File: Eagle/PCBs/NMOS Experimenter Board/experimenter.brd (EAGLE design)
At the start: 77.5 x 99.1 mm, 1209 parts, among them Q10 2N7002, Q11 2N7002, Q12 2N7002, Q13 2N7002, Q14 2N7002, Q15 2N7002, Q16 2N7002, Q17 2N7002, Q18 2N7002, Q19 2N7002, Q2 2N7002, Q20 2N7002, Q21 2N7002, Q22 2N7002, Q23 2N7002, Q24 2N7002, Q25 2N7002, Q26 2N7002, Q27 2N7002, Q28 2N7002, Q29 2N7002, Q3 2N7002, Q30 2N7002, Q31 2N7002, Q32 2N7002, Q33 2N7002, Q34 2N7002, Q35 2N7002, Q36 2N7002, Q37 2N7002, Q38 2N7002, Q39 2N7002, Q4 2N7002, Q40 2N7002, Q41 2N7002, Q42 2N7002, Q43 2N7002, Q44 2N7002, Q45 2N7002, Q46 2N7002, Q47 2N7002, Q48 2N7002, Q49 2N7002, Q5 2N7002, Q50 2N7002, Q51 2N7002, Q52 2N7002, Q53 2N7002, Q54 2N7002, Q55 2N7002, Q56 2N7002, Q57 2N7002, Q58 2N7002, Q59 2N7002, Q6 2N7002, Q60 2N7002, Q61 2N7002, Q62 2N7002, Q63 2N7002, Q64 2N7002, Q65 2N7002, Q66 2N7002, Q67 2N7002, Q68 2N7002, Q69 2N7002, Q7 2N7002, Q70 2N7002, Q71 2N7002, Q72 2N7002, Q73 2N7002, Q8 2N7002, Q9 2N7002, U1 74HC14PW, U2 74HC14PW

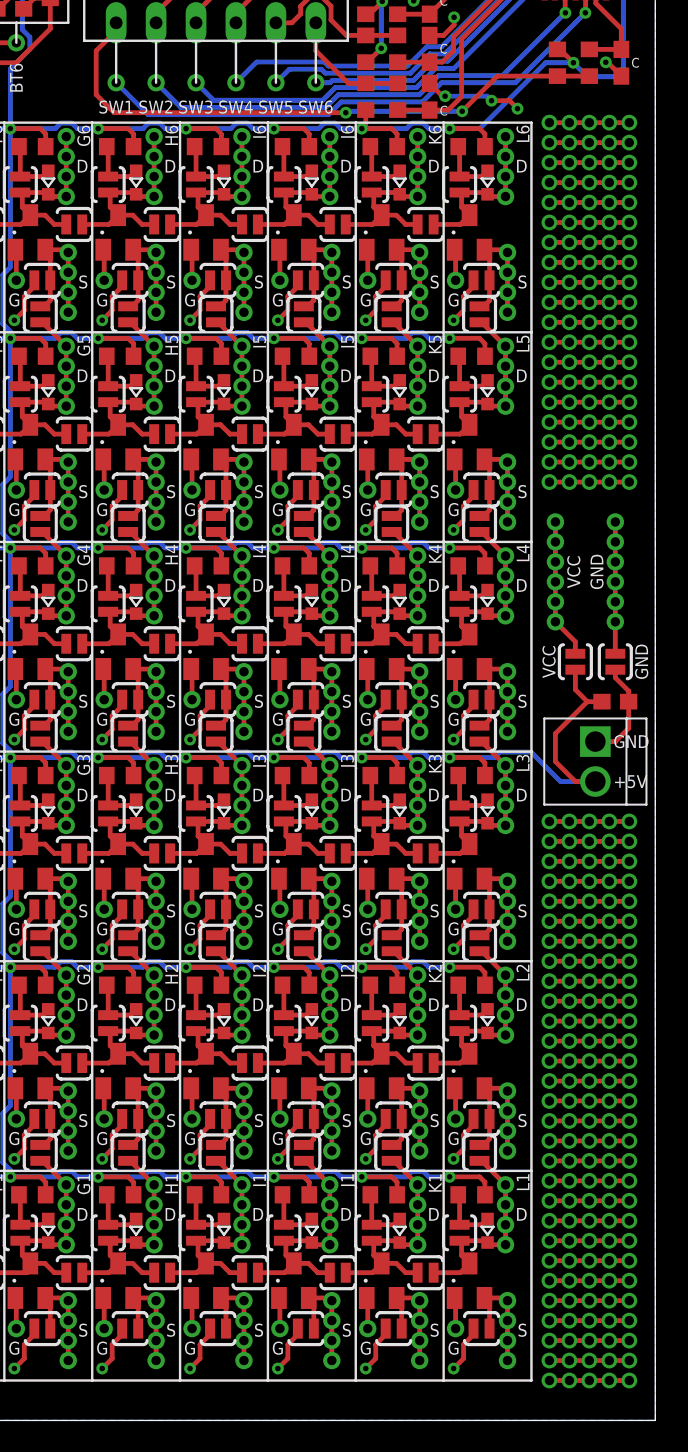
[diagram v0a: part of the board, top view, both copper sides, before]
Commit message: Added amazing protoboard area.
https://www.eevblog.com/forum/manufacture/improved-protoboardperfboard-for-direct-soic-mounting/
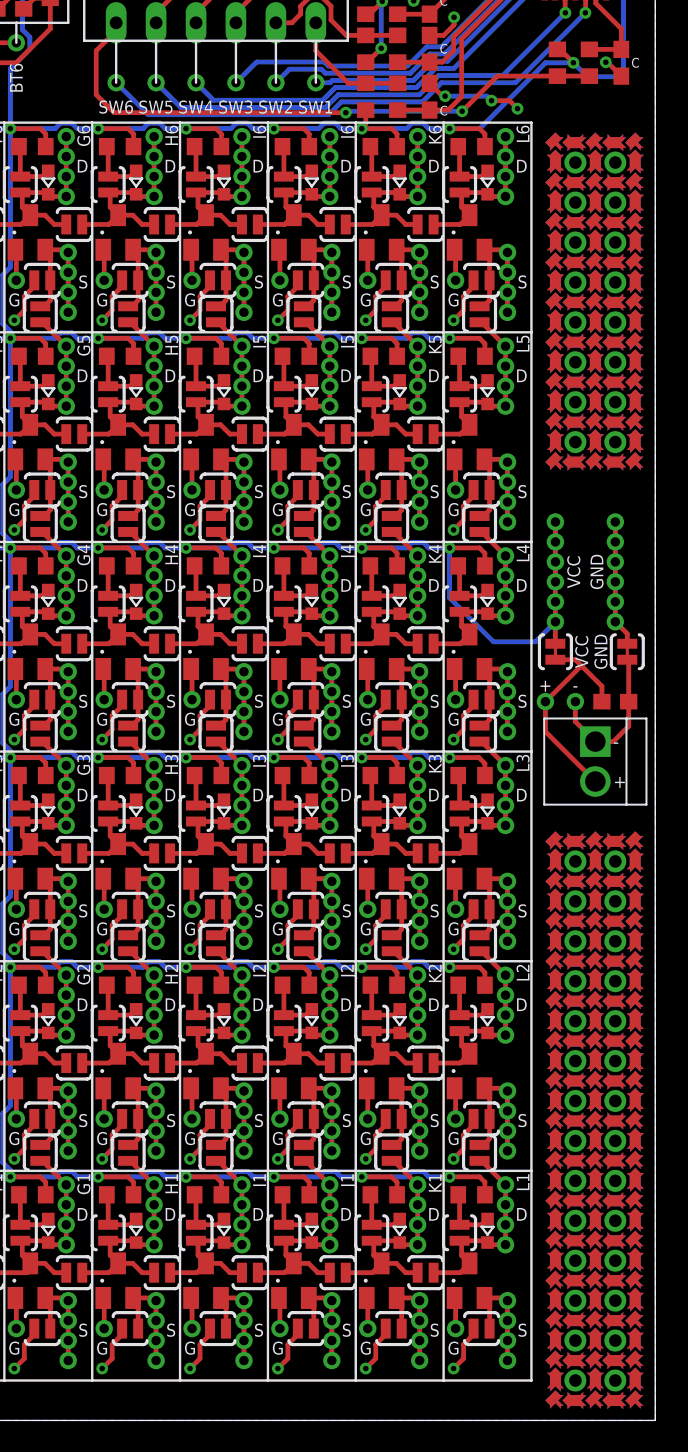
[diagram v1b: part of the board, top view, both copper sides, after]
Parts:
- added U$1, U$101, U$105, U$109, U$113, U$117, U$121, U$125, U$162, U$166, U$170, U$174, U$182, U$186, U$190, U$194, U$198, U$202, U$206, U$21, U$210, U$214, U$218, U$222, U$226, U$25, U$29, U$33, U$37, U$41, U$45, U$49, U$53, U$57, U$61, U$65, U$69, U$73, U$77, U$81, U$85, U$89, U$93, U$97: PROTOPADTHT, ellajameson-core:PROTOPAD-THT
- added U$10, U$100, U$104, U$108, U$112, U$116, U$12, U$120, U$124, U$128, U$130, U$132, U$134, U$136, U$138, U$14, U$140, U$142, U$144, U$145, U$147, U$149, U$151, U$153, U$154, U$156, U$158, U$16, U$160, U$165, U$169, U$173, U$177, U$178, U$18, U$180, U$185, U$189, U$193, U$197, U$20, U$201, U$205, U$209, U$213, U$217, U$221, U$225, U$229, U$230, U$24, U$28, U$32, U$36, U$4, U$40, U$44, U$48, U$52, U$56, U$6, U$60, U$64, U$68, U$72, U$76, U$8, U$80, U$84, U$88, U$92, U$96: (no value), ellajameson-core:PROTOPAD-CENTER
- added U$102, U$103, U$106, U$107, U$11, U$110, U$111, U$114, U$115, U$118, U$119, U$122, U$123, U$126, U$127, U$129, U$13, U$131, U$133, U$135, U$137, U$139, U$141, U$143, U$146, U$148, U$15, U$150, U$152, U$155, U$157, U$159, U$161, U$163, U$164, U$167, U$168, U$17, U$171, U$172, U$175, U$176, U$179, U$181, U$183, U$184, U$187, U$188, U$19, U$191, U$192, U$195, U$196, U$199, U$2, U$200, U$203, U$204, U$207, U$208, U$211, U$212, U$215, U$216, U$219, U$22, U$220, U$223, U$224, U$227, U$228, U$23, U$26, U$27, U$3, U$30, U$31, U$34, U$35, U$38, U$39, U$42, U$43, U$46, U$47, U$5, U$50, U$51, U$54, U$55, U$58, U$59, U$62, U$63, U$66, U$67, U$7, U$70, U$71, U$74, U$75, U$78, U$79, U$82, U$83, U$86, U$87, U$9, U$90, U$91, U$94, U$95, U$98, U$99: (no value), ellajameson-core:PROTOPAD-BETWEEN
- added VIN+1, VIN-1: TPWIRE, ellajameson-core:TP_TH_WIRE
- SJ1, SJ2: value SJ_NO -> SJ_NC; device ellajameson-core:SJ_2S-NO -> ellajameson-core:SJ_2S-TRACE
- moved SJ1 3.86 mm to (71.1, 48.9), turned to 90 degrees
- moved SJ2 3.36 mm to (75.7, 48.9)
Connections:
- removed net N$303: SJ2.2, VCC1.TP, VCC2.TP, VCC3.TP, VCC4.TP, VCC5.TP, VCC6.TP
- removed net N$304: SJ1.1, VSS1.TP, VSS2.TP, VSS3.TP, VSS4.TP, VSS5.TP, VSS6.TP
- new net N$321: C4.1, J1.P$1, SJ2.1, VIN-1.TP
- new net N$322: C4.2, J1.P$2, SJ1.1, VIN+1.TP
- net GND: now also SJ2.2, VSS1.TP, VSS2.TP, VSS3.TP, VSS4.TP, VSS5.TP, VSS6.TP; no longer C4.1, J1.P$1, SJ1.2
- net VCC: now also SJ1.2, VCC1.TP, VCC2.TP, VCC3.TP, VCC4.TP, VCC5.TP, VCC6.TP; no longer C4.2, J1.P$2, SJ2.1
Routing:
- net N$322: track 0.00 -> 14.3 mm
- net N$321: track 0.00 -> 9.86 mm
- net N$303: track 8.91 -> 0.00 mm
- net N$304: track 8.38 -> 0.00 mm
- net BB9: track 5.08 -> 0.00 mm, vias 5 -> 0
- net BB8: track 5.08 -> 0.00 mm, vias 5 -> 0
- net BB7: track 5.08 -> 0.00 mm, vias 5 -> 0
- net BB6: track 5.08 -> 0.00 mm, vias 5 -> 0
- net BB5: track 5.08 -> 0.00 mm, vias 5 -> 0
- net BB48: track 5.08 -> 0.00 mm, vias 5 -> 0
- net BB47: track 5.08 -> 0.00 mm, vias 5 -> 0
- net BB46: track 5.08 -> 0.00 mm, vias 5 -> 0
- net BB45: track 5.08 -> 0.00 mm, vias 5 -> 0
- net BB44: track 5.08 -> 0.00 mm, vias 5 -> 0
- net BB43: track 5.08 -> 0.00 mm, vias 5 -> 0
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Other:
- board text added: "+"
- board text added: "-"
- board text removed: "+5V"

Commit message: Start rework on experimenter
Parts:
- removed C10, C12, C13, C14, C15, C6, C8: 0.1u, ellajameson-core:C0603
- removed D10, D11, D12, D13, D14, D15, D16, D17, D18, D19, D2, D20, D21, D22, D23, D24, D25, D26, D27, D28, D29, D3, D30, D31, D32, D33, D34, D35, D36, D37, D38, D39, D4, D40, D41, D42, D43, D44, D45, D46, D47, D48, D49, D5, D50, D51, D52, D53, D54, D55, D56, D57, D58, D59, D6, D60, D61, D62, D63, D64, D65, D66, D67, D68, D69, D7, D70, D71, D72, D73, D8, D9: (no value), ellajameson-core:CHIP-LED0603
- removed DRAINA10, DRAINA11, DRAINA12, DRAINA13, DRAINA14, DRAINA15, DRAINA16, DRAINA17, DRAINA18, DRAINA19, DRAINA2, DRAINA20, DRAINA21, DRAINA22, DRAINA23, DRAINA24, DRAINA25, DRAINA26, DRAINA27, DRAINA28, DRAINA29, DRAINA3, DRAINA30, DRAINA31, DRAINA32, DRAINA33, DRAINA34, DRAINA35, DRAINA36, DRAINA37, DRAINA38, DRAINA39, DRAINA4, DRAINA40, DRAINA41, DRAINA42, DRAINA43, DRAINA44, DRAINA45, DRAINA46, DRAINA47, DRAINA48, DRAINA49, DRAINA5, DRAINA50, DRAINA51, DRAINA52, DRAINA53, DRAINA54, DRAINA55, DRAINA56, DRAINA57, DRAINA58, DRAINA59, DRAINA6, DRAINA60, DRAINA61, DRAINA62, DRAINA63, DRAINA64, DRAINA65, DRAINA66, DRAINA67, DRAINA68, DRAINA69, DRAINA7, DRAINA70, DRAINA71, DRAINA72, DRAINA73, DRAINA8, DRAINA9, DRAINB10, DRAINB11, DRAINB12, DRAINB13, DRAINB14, DRAINB15, DRAINB16, DRAINB17, DRAINB18, DRAINB19, DRAINB2, DRAINB20, DRAINB21, DRAINB22, DRAINB23, DRAINB24, DRAINB25, DRAINB26, DRAINB27, DRAINB28, DRAINB29, DRAINB3, DRAINB30, DRAINB31, DRAINB32, DRAINB33, DRAINB34, DRAINB35, DRAINB36, DRAINB37, DRAINB38, DRAINB39, DRAINB4, DRAINB40, DRAINB41, DRAINB42, DRAINB43, DRAINB44, DRAINB45, DRAINB46, DRAINB47, DRAINB48, DRAINB49, DRAINB5, DRAINB50, DRAINB51, DRAINB52, DRAINB53, DRAINB54, DRAINB55, DRAINB56, DRAINB57, DRAINB58, DRAINB59, DRAINB6, DRAINB60, DRAINB61, DRAINB62, DRAINB63, DRAINB64, DRAINB65, DRAINB66, DRAINB67, DRAINB68, DRAINB69, DRAINB7, DRAINB70, DRAINB71, DRAINB72, DRAINB73, DRAINB8, DRAINB9, DRAINC10, DRAINC11, DRAINC12, DRAINC13, DRAINC14, DRAINC15, DRAINC16, DRAINC17, DRAINC18, DRAINC19, DRAINC2, DRAINC20, DRAINC21, DRAINC22, DRAINC23, DRAINC24, DRAINC25, DRAINC26, DRAINC27, DRAINC28, DRAINC29, DRAINC3, DRAINC30, DRAINC31, DRAINC32, DRAINC33, DRAINC34, DRAINC35, DRAINC36, DRAINC37, DRAINC38, DRAINC39, DRAINC4, DRAINC40, DRAINC41, DRAINC42, DRAINC43, DRAINC44, DRAINC45, DRAINC46, DRAINC47, DRAINC48, DRAINC49, DRAINC5, DRAINC50, DRAINC51, DRAINC52, DRAINC53, DRAINC54, DRAINC55, DRAINC56, DRAINC57, DRAINC58, DRAINC59, DRAINC6, DRAINC60, DRAINC61, DRAINC62, DRAINC63, DRAINC64, DRAINC65, DRAINC66, DRAINC67, DRAINC68, DRAINC69, DRAINC7, DRAINC70, DRAINC71, DRAINC72, DRAINC73, DRAINC8, DRAINC9, DRAIND10, DRAIND11, DRAIND12, DRAIND13, DRAIND14, DRAIND15, DRAIND16, DRAIND17, DRAIND18, DRAIND19, DRAIND2, DRAIND20, DRAIND21, DRAIND22, DRAIND23, DRAIND24, DRAIND25, DRAIND26, DRAIND27, DRAIND28, DRAIND29, DRAIND3, DRAIND30, DRAIND31, DRAIND32, DRAIND33, DRAIND34, DRAIND35, DRAIND36, DRAIND37, DRAIND38, DRAIND39, DRAIND4, DRAIND40, DRAIND41, DRAIND42, DRAIND43, DRAIND44, DRAIND45, DRAIND46, DRAIND47, DRAIND48, DRAIND49, DRAIND5, DRAIND50, DRAIND51, DRAIND52, DRAIND53, DRAIND54, DRAIND55, DRAIND56, DRAIND57, DRAIND58, DRAIND59, DRAIND6, DRAIND60, DRAIND61, DRAIND62, DRAIND63, DRAIND64, DRAIND65, DRAIND66, DRAIND67, DRAIND68, DRAIND69, DRAIND7, DRAIND70, DRAIND71, DRAIND72, DRAIND73, DRAIND8, DRAIND9, GATE10, GATE11, GATE12, GATE13, GATE14, GATE15, GATE16, GATE17, GATE18, GATE19, GATE2, GATE20, GATE21, GATE22, GATE23, GATE24, GATE25, GATE26, GATE27, GATE28, GATE29, GATE3, GATE30, GATE31, GATE32, GATE33, GATE34, GATE35, GATE36, GATE37, GATE38, GATE39, GATE4, GATE40, GATE41, GATE42, GATE43, GATE44, GATE45, GATE46, GATE47, GATE48, GATE49, GATE5, GATE50, GATE51, GATE52, GATE53, GATE54, GATE55, GATE56, GATE57, GATE58, GATE59, GATE6, GATE60, GATE61, GATE62, GATE63, GATE64, GATE65, GATE66, GATE67, GATE68, GATE69, GATE7, GATE70, GATE71, GATE72, GATE73, GATE8, GATE9, SO1, SO2, SO3, SO4, SO5, SO6, SOURCEA10, SOURCEA11, SOURCEA12, SOURCEA13, SOURCEA14, SOURCEA15, SOURCEA16, SOURCEA17, SOURCEA18, SOURCEA19, SOURCEA2, SOURCEA20, SOURCEA21, SOURCEA22, SOURCEA23, SOURCEA24, SOURCEA25, SOURCEA26, SOURCEA27, SOURCEA28, SOURCEA29, SOURCEA3, SOURCEA30, SOURCEA31, SOURCEA32, SOURCEA33, SOURCEA34, SOURCEA35, SOURCEA36, SOURCEA37, SOURCEA38, SOURCEA39, SOURCEA4, SOURCEA40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: TPWIRE, ellajameson-core:TP_TH_WIRE
- removed JD10, JD11, JD12, JD13, JD14, JD17, JD18, JD19, JD2, JD20, JD21, JD22, JD23, JD24, JD25, JD26, JD27, JD28, JD29, JD3, JD30, JD31, JD32, JD33, JD34, JD35, JD36, JD37, JD38, JD39, JD4, JD40, JD41, JD42, JD43, JD44, JD45, JD46, JD47, JD48, JD49, JD5, JD50, JD51, JD52, JD53, JD54, JD55, JD56, JD57, JD58, JD59, JD6, JD60, JD61, JD62, JD63, JD64, JD65, JD66, JD68, JD7, JD70, JD72, JD8, JD9, JN10, JN11, JN12, JN13, JN14, JN15, JN16, JN17, JN18, JN19, JN2, JN20, JN21, JN22, JN23, JN24, JN25, JN26, JN27, JN28, JN29, JN3, JN30, JN31, JN32, JN33, JN34, JN35, JN36, JN37, JN38, JN39, JN4, JN40, JN41, JN42, JN43, JN44, JN45, JN46, JN47, JN48, JN49, JN5, JN50, JN51, JN52, JN53, JN54, JN55, JN56, JN57, JN58, JN59, JN6, JN60, JN61, JN62, JN63, JN64, JN65, JN66, JN67, JN68, JN69, JN7, JN70, JN71, JN72, JN73, JN8, JN9, JP10, JP11, JP12, JP13, JP14, JP15, JP16, JP17, JP18, JP19, JP2, JP20, JP21, JP22, JP23, JP24, JP25, JP26, JP27, JP28, JP29, JP3, JP30, JP31, JP32, JP33, JP34, JP35, JP36, JP37, JP38, JP39, JP4, JP40, JP41, JP42, JP43, JP44, JP45, JP46, JP47, JP48, JP49, JP5, JP50, JP51, JP52, JP53, JP54, JP55, JP56, JP57, JP58, JP59, JP6, JP60, JP61, JP62, JP63, JP64, JP65, JP66, JP67, JP68, JP69, JP7, JP70, JP71, JP72, JP73, JP8, JP9, JS10, JS11, JS12, JS13, JS16, JS17, JS26, JS27, JS28, JS29, JS30, JS31, JS32, JS33, JS34, JS35, JS36, JS37, JS38, JS39, JS4, JS40, JS41, JS42, JS43, JS44, JS45, JS46, JS47, JS48, JS49, JS5, JS50, JS51, JS52, JS53, JS54, JS55, JS56, JS57, JS58, JS59, JS6, JS60, JS61, JS62, JS63, JS64, JS65, JS66, JS67, JS68, JS69, JS7, JS70, JS71, JS72, JS73, JS8, JS9: SJ_NO, ellajameson-core:SJ_2S-NO
- removed Q10, Q11, Q12, Q13, Q14, Q15, Q16, Q17, Q18, Q19, Q2, Q20, Q21, Q22, Q23, Q24, Q25, Q26, Q27, Q28, Q29, Q3, Q30, Q31, Q32, Q33, Q34, Q35, Q36, Q37, Q38, Q39, Q4, Q40, Q41, Q42, Q43, Q44, Q45, Q46, Q47, Q48, Q49, Q5, Q50, Q51, Q52, Q53, Q54, Q55, Q56, Q57, Q58, Q59, Q6, Q60, Q61, Q62, Q63, Q64, Q65, Q66, Q67, Q68, Q69, Q7, Q70, Q71, Q72, Q73, Q8, Q9: 2N7002, ellajameson-core:SOT23
- removed R1, R74, R79, R80, R83, R84, R87, R88, R91, R92, R95, R96: 10k, ellajameson-core:R0603
- removed R10, R11, R12, R13, R14, R15, R16, R17, R18, R19, R2, R20, R21, R22, R23, R24, R25, R26, R27, R28, R29, R3, R30, R31, R32, R33, R34, R35, R36, R37, R38, R39, R4, R40, R41, R42, R43, R44, R45, R46, R47, R48, R49, R5, R50, R51, R52, R53, R54, R55, R56, R57, R58, R59, R6, R60, R61, R62, R63, R64, R65, R66, R67, R68, R69, R7, R70, R71, R72, R73, R8, R9: (no value), ellajameson-core:R0603
- removed U$1, U$101, U$105, U$109, U$113, U$117, U$121, U$125, U$162, U$166, U$170, U$174, U$182, U$186, U$190, U$194, U$198, U$202, U$206, U$21, U$210, U$214, U$218, U$222, U$226, U$25, U$29, U$33, U$37, U$41, U$45, U$49, U$53, U$57, U$61, U$65, U$69, U$73, U$77, U$81, U$85, U$89, U$93, U$97: PROTOPADTHT, ellajameson-core:PROTOPAD-THT
- removed U$10, U$100, U$104, U$108, U$112, U$116, U$12, U$120, U$124, U$128, U$130, U$132, U$134, U$136, U$138, U$14, U$140, U$142, U$144, U$145, U$147, U$149, U$151, U$153, U$154, U$156, U$158, U$16, U$160, U$165, U$169, U$173, U$177, U$178, U$18, U$180, U$185, U$189, U$193, U$197, U$20, U$201, U$205, U$209, U$213, U$217, U$221, U$225, U$229, U$230, U$24, U$28, U$32, U$36, U$4, U$40, U$44, U$48, U$52, U$56, U$6, U$60, U$64, U$68, U$72, U$76, U$8, U$80, U$84, U$88, U$92, U$96: (no value), ellajameson-core:PROTOPAD-CENTER
- removed U$102, U$103, U$106, U$107, U$11, U$110, U$111, U$114, U$115, U$118, U$119, U$122, U$123, U$126, U$127, U$129, U$13, U$131, U$133, U$135, U$137, U$139, U$141, U$143, U$146, U$148, U$15, U$150, U$152, U$155, U$157, U$159, U$161, U$163, U$164, U$167, U$168, U$17, U$171, U$172, U$175, U$176, U$179, U$181, U$183, U$184, U$187, U$188, U$19, U$191, U$192, U$195, U$196, U$199, U$2, U$200, U$203, U$204, U$207, U$208, U$211, U$212, U$215, U$216, U$219, U$22, U$220, U$223, U$224, U$227, U$228, U$23, U$26, U$27, U$3, U$30, U$31, U$34, U$35, U$38, U$39, U$42, U$43, U$46, U$47, U$5, U$50, U$51, U$54, U$55, U$58, U$59, U$62, U$63, U$66, U$67, U$7, U$70, U$71, U$74, U$75, U$78, U$79, U$82, U$83, U$86, U$87, U$9, U$90, U$91, U$94, U$95, U$98, U$99: (no value), ellajameson-core:PROTOPAD-BETWEEN
- removed U2: 74HC14PW, ellajameson-core:TSSOP14
- B1, B2, B3, B4, B5, B6, VCC1, VCC2, VCC3, VIN+1, VIN-1, VSS1, VSS2, VSS3: value TPWIRE -> TPTHT; device ellajameson-core:TP_TH_WIRE -> ellajameson-core:PROTOPAD-THT
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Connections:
- removed net N$1: D2.A, JP2.2, R2.1
- removed net N$10: D3.C, DRAINA3.TP, DRAINB3.TP, DRAINC3.TP, DRAIND3.TP, JD2.1, JD3.2, JP3.1, JS5.1, Q3.3
- removed net N$100: GATE25.TP, Q25.1
- removed net N$101: D26.A, JP26.2, R26.1
- removed net N$102: D26.C, DRAINA26.TP, DRAINB26.TP, DRAINC26.TP, DRAIND26.TP, JD26.2, JP26.1, JS34.1, Q26.3
- removed net N$103: JN26.2, JS26.2, Q26.2, SOURCEA26.TP, SOURCEB26.TP, SOURCEC26.TP, SOURCED26.TP
- removed net N$104: GATE26.TP, Q26.1
- removed net N$105: D27.A, JP27.2, R27.1
- removed net N$106: D27.C, DRAINA27.TP, DRAINB27.TP, DRAINC27.TP, DRAIND27.TP, JD26.1, JD27.2, JP27.1, JS35.1, Q27.3
- removed net N$107: JN27.2, JS27.2, Q27.2, SOURCEA27.TP, SOURCEB27.TP, SOURCEC27.TP, SOURCED27.TP
- removed net N$108: GATE27.TP, Q27.1
- removed net N$109: D28.A, JP28.2, R28.1
- removed net N$11: JN3.2, Q3.2, SOURCEA3.TP, SOURCEB3.TP, SOURCEC3.TP, SOURCED3.TP
- removed net N$110: D28.C, DRAINA28.TP, DRAINB28.TP, DRAINC28.TP, DRAIND28.TP, JD27.1, JD28.2, JP28.1, JS36.1, Q28.3
- removed net N$111: JN28.2, JS28.2, Q28.2, SOURCEA28.TP, SOURCEB28.TP, SOURCEC28.TP, SOURCED28.TP
- removed net N$112: GATE28.TP, Q28.1
- removed net N$113: D29.A, JP29.2, R29.1
- removed net N$114: D29.C, DRAINA29.TP, DRAINB29.TP, DRAINC29.TP, DRAIND29.TP, JD28.1, JD29.2, JP29.1, JS37.1, Q29.3
- removed net N$115: JN29.2, JS29.2, Q29.2, SOURCEA29.TP, SOURCEB29.TP, SOURCEC29.TP, SOURCED29.TP
- removed net N$116: GATE29.TP, Q29.1
- removed net N$117: D30.A, JP30.2, R30.1
- removed net N$118: D30.C, DRAINA30.TP, DRAINB30.TP, DRAINC30.TP, DRAIND30.TP, JD29.1, JD30.2, JP30.1, JS38.1, Q30.3
- removed net N$119: JN30.2, JS30.2, Q30.2, SOURCEA30.TP, SOURCEB30.TP, SOURCEC30.TP, SOURCED30.TP
- removed net N$12: GATE3.TP, Q3.1
- removed net N$120: GATE30.TP, Q30.1
- removed net N$121: D31.A, JP31.2, R31.1
- removed net N$122: D31.C, DRAINA31.TP, DRAINB31.TP, DRAINC31.TP, DRAIND31.TP, JD30.1, JD31.2, JP31.1, JS39.1, Q31.3
- removed net N$123: JN31.2, JS31.2, Q31.2, SOURCEA31.TP, SOURCEB31.TP, SOURCEC31.TP, SOURCED31.TP
- removed net N$124: GATE31.TP, Q31.1
- removed net N$125: D32.A, JP32.2, R32.1
- removed net N$126: D32.C, DRAINA32.TP, DRAINB32.TP, DRAINC32.TP, DRAIND32.TP, JD31.1, JD32.2, JP32.1, JS40.1, Q32.3
- removed net N$127: JN32.2, JS32.2, Q32.2, SOURCEA32.TP, SOURCEB32.TP, SOURCEC32.TP, SOURCED32.TP
- removed net N$128: GATE32.TP, Q32.1
- removed net N$129: D33.A, JP33.2, R33.1
- removed net N$13: D4.A, JP4.2, R4.1
- removed net N$130: D33.C, DRAINA33.TP, DRAINB33.TP, DRAINC33.TP, DRAIND33.TP, JD32.1, JD33.2, JP33.1, JS41.1, Q33.3
- removed net N$131: JN33.2, JS33.2, Q33.2, SOURCEA33.TP, SOURCEB33.TP, SOURCEC33.TP, SOURCED33.TP
- removed net N$132: GATE33.TP, Q33.1
- removed net N$133: D34.A, JP34.2, R34.1
- removed net N$134: D34.C, DRAINA34.TP, DRAINB34.TP, DRAINC34.TP, DRAIND34.TP, JD34.2, JP34.1, JS42.1, Q34.3
- removed net N$135: JN34.2, JS34.2, Q34.2, SOURCEA34.TP, SOURCEB34.TP, SOURCEC34.TP, SOURCED34.TP
- removed net N$136: GATE34.TP, Q34.1
- removed net N$137: D35.A, JP35.2, R35.1
- removed net N$138: D35.C, DRAINA35.TP, DRAINB35.TP, DRAINC35.TP, DRAIND35.TP, JD34.1, JD35.2, JP35.1, JS43.1, Q35.3
- removed net N$139: JN35.2, JS35.2, Q35.2, SOURCEA35.TP, SOURCEB35.TP, SOURCEC35.TP, SOURCED35.TP
- removed net N$14: D4.C, DRAINA4.TP, DRAINB4.TP, DRAINC4.TP, DRAIND4.TP, JD33.1, JD4.2, JP4.1, JS6.1, Q4.3
- removed net N$140: GATE35.TP, Q35.1
- removed net N$141: D36.A, JP36.2, R36.1
- removed net N$142: D36.C, DRAINA36.TP, DRAINB36.TP, DRAINC36.TP, DRAIND36.TP, JD35.1, JD36.2, JP36.1, JS44.1, Q36.3
- removed net N$143: JN36.2, JS36.2, Q36.2, SOURCEA36.TP, SOURCEB36.TP, SOURCEC36.TP, SOURCED36.TP
- removed net N$144: GATE36.TP, Q36.1
- removed net N$145: D37.A, JP37.2, R37.1
- removed net N$146: D37.C, DRAINA37.TP, DRAINB37.TP, DRAINC37.TP, DRAIND37.TP, JD36.1, JD37.2, JP37.1, JS45.1, Q37.3
- removed net N$147: JN37.2, JS37.2, Q37.2, SOURCEA37.TP, SOURCEB37.TP, SOURCEC37.TP, SOURCED37.TP
- removed net N$148: GATE37.TP, Q37.1
- removed net N$149: D38.A, JP38.2, R38.1
- removed net N$15: JN4.2, JS4.2, Q4.2, SOURCEA4.TP, SOURCEB4.TP, SOURCEC4.TP, SOURCED4.TP
- removed net N$150: D38.C, DRAINA38.TP, DRAINB38.TP, DRAINC38.TP, DRAIND38.TP, JD37.1, JD38.2, JP38.1, JS46.1, Q38.3
- removed net N$151: JN38.2, JS38.2, Q38.2, SOURCEA38.TP, SOURCEB38.TP, SOURCEC38.TP, SOURCED38.TP
- removed net N$152: GATE38.TP, Q38.1
- removed net N$153: D39.A, JP39.2, R39.1
- removed net N$154: D39.C, DRAINA39.TP, DRAINB39.TP, DRAINC39.TP, DRAIND39.TP, JD38.1, JD39.2, JP39.1, JS47.1, Q39.3
- removed net N$155: JN39.2, JS39.2, Q39.2, SOURCEA39.TP, SOURCEB39.TP, SOURCEC39.TP, SOURCED39.TP
- removed net N$156: GATE39.TP, Q39.1
- removed net N$157: D40.A, JP40.2, R40.1
- removed net N$158: D40.C, DRAINA40.TP, DRAINB40.TP, DRAINC40.TP, DRAIND40.TP, JD39.1, JD40.2, JP40.1, JS48.1, Q40.3
- removed net N$159: JN40.2, JS40.2, Q40.2, SOURCEA40.TP, SOURCEB40.TP, SOURCEC40.TP, SOURCED40.TP
- removed net N$16: GATE4.TP, Q4.1
- removed net N$160: GATE40.TP, Q40.1
- removed net N$161: D41.A, JP41.2, R41.1
- removed net N$162: D41.C, DRAINA41.TP, DRAINB41.TP, DRAINC41.TP, DRAIND41.TP, JD40.1, JD41.2, JP41.1, JS49.1, Q41.3
- removed net N$163: JN41.2, JS41.2, Q41.2, SOURCEA41.TP, SOURCEB41.TP, SOURCEC41.TP, SOURCED41.TP
- removed net N$164: GATE41.TP, Q41.1
- removed net N$165: D42.A, JP42.2, R42.1
- removed net N$166: D42.C, DRAINA42.TP, DRAINB42.TP, DRAINC42.TP, DRAIND42.TP, JD42.2, JP42.1, JS50.1, Q42.3
- removed net N$167: JN42.2, JS42.2, Q42.2, SOURCEA42.TP, SOURCEB42.TP, SOURCEC42.TP, SOURCED42.TP
- removed net N$168: GATE42.TP, Q42.1
- removed net N$169: D43.A, JP43.2, R43.1
- removed net N$17: D5.A, JP5.2, R5.1
- removed net N$170: D43.C, DRAINA43.TP, DRAINB43.TP, DRAINC43.TP, DRAIND43.TP, JD42.1, JD43.2, JP43.1, JS51.1, Q43.3
- removed net N$171: JN43.2, JS43.2, Q43.2, SOURCEA43.TP, SOURCEB43.TP, SOURCEC43.TP, SOURCED43.TP
- removed net N$172: GATE43.TP, Q43.1
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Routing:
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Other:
- board text added: "IN1"
- board text added: "IN2"
- board text added: "IN3"
- board text added: "IN4"
- board text added: "IN5"
- board text added: "IN6"
- board text removed: "A1"
- board text removed: "A2"
- board text removed: "A3"
- board text removed: "A4"
- board text removed: "A5"
- board text removed: "A6"
- board text removed: "B1"
- board text removed: "B2"
- board text removed: "B3"
- board text removed: "B4"
- board text removed: "B5"
- board text removed: "B6"
- board text removed: "BT1"
- board text removed: "BT2"
- board text removed: "BT3"
- board text removed: "BT4"
- board text removed: "BT5"
- board text removed: "BT6"
- board text removed: "C1"
- board text removed: "C2"
- board text removed: "C3"
- board text removed: "C4"
- board text removed: "C5"
- board text removed: "C6"
- board text removed: "D"
- board text removed: "D1"
- board text removed: "D2"
- board text removed: "D3"
- board text removed: "D4"
- board text removed: "D5"
- board text removed: "D6"
- board text removed: "E1"
- board text removed: "E2"
- board text removed: "E3"
- board text removed: "E4"
- board text removed: "E5"
- board text removed: "E6"
- board text removed: "F1"
- board text removed: "F2"
- board text removed: "F3"
- board text removed: "F4"
- board text removed: "F5"
- board text removed: "F6"
- board text removed: "G"
- board text removed: "G1"
- board text removed: "G2"
- board text removed: "G3"
- board text removed: "G4"
- board text removed: "G5"
- board text removed: "G6"
- board text removed: "H1"
- board text removed: "H2"
- board text removed: "H3"
- board text removed: "H4"
- board text removed: "H5"
- board text removed: "H6"
- board text removed: "I1"
- board text removed: "I2"
- board text removed: "I3"
- board text removed: "I4"
- board text removed: "I5"
- board text removed: "I6"
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
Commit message: Wow, 92 transistors and 8 LEDs
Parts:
- added D2, D3, D4, D5, D6, D7, D8, D9: (no value), ellajameson-core:CHIP-LED0603
- added DRAINA100, DRAINA101, DRAINA102, DRAINA103, DRAINA104, DRAINA105, DRAINA106, DRAINA107, DRAINA108, DRAINA109, DRAINA110, DRAINA111, DRAINA112, DRAINA2, DRAINA21, DRAINA22, DRAINA23, DRAINA24, DRAINA25, DRAINA26, DRAINA27, DRAINA28, DRAINA29, DRAINA3, DRAINA30, DRAINA31, DRAINA32, DRAINA33, DRAINA34, DRAINA35, DRAINA36, DRAINA37, DRAINA38, DRAINA39, DRAINA4, DRAINA40, DRAINA41, DRAINA42, DRAINA43, DRAINA44, DRAINA45, DRAINA46, DRAINA47, DRAINA48, DRAINA49, DRAINA5, DRAINA50, DRAINA51, DRAINA52, DRAINA53, DRAINA54, DRAINA55, DRAINA56, DRAINA57, DRAINA58, DRAINA59, DRAINA60, DRAINA61, DRAINA62, DRAINA63, DRAINA64, DRAINA65, DRAINA66, DRAINA67, DRAINA68, DRAINA69, DRAINA70, DRAINA71, DRAINA72, DRAINA73, DRAINA74, DRAINA75, DRAINA76, DRAINA77, DRAINA78, DRAINA79, DRAINA80, DRAINA81, DRAINA82, DRAINA83, DRAINA84, DRAINA85, DRAINA86, DRAINA87, DRAINA88, DRAINA89, DRAINA90, DRAINA91, DRAINA92, DRAINA93, DRAINA94, DRAINA95, DRAINA96, DRAINA97, DRAINA98, DRAINA99, DRAINB100, DRAINB101, DRAINB102, DRAINB103, DRAINB104, DRAINB105, DRAINB106, DRAINB107, DRAINB108, DRAINB109, DRAINB110, DRAINB111, DRAINB112, DRAINB2, DRAINB21, DRAINB22, DRAINB23, DRAINB24, DRAINB25, DRAINB26, DRAINB27, DRAINB28, DRAINB29, DRAINB3, DRAINB30, DRAINB31, DRAINB32, DRAINB33, DRAINB34, DRAINB35, DRAINB36, DRAINB37, DRAINB38, DRAINB39, DRAINB4, DRAINB40, DRAINB41, DRAINB42, DRAINB43, DRAINB44, DRAINB45, DRAINB46, DRAINB47, DRAINB48, DRAINB49, DRAINB5, DRAINB50, DRAINB51, DRAINB52, DRAINB53, DRAINB54, DRAINB55, DRAINB56, DRAINB57, DRAINB58, DRAINB59, DRAINB60, DRAINB61, DRAINB62, DRAINB63, DRAINB64, DRAINB65, DRAINB66, DRAINB67, DRAINB68, DRAINB69, DRAINB70, DRAINB71, DRAINB72, DRAINB73, DRAINB74, DRAINB75, DRAINB76, DRAINB77, DRAINB78, DRAINB79, DRAINB80, DRAINB81, DRAINB82, DRAINB83, DRAINB84, DRAINB85, DRAINB86, DRAINB87, DRAINB88, DRAINB89, DRAINB90, DRAINB91, DRAINB92, DRAINB93, DRAINB94, DRAINB95, DRAINB96, DRAINB97, DRAINB98, DRAINB99, GATEA100, GATEA101, GATEA102, GATEA103, GATEA104, GATEA105, GATEA106, GATEA107, GATEA108, GATEA109, GATEA110, GATEA111, GATEA112, GATEA2, GATEA21, GATEA22, GATEA23, GATEA24, GATEA25, GATEA26, GATEA27, GATEA28, GATEA29, GATEA3, GATEA30, GATEA31, GATEA32, GATEA33, GATEA34, GATEA35, GATEA36, GATEA37, GATEA38, GATEA39, GATEA4, GATEA40, GATEA41, GATEA42, GATEA43, GATEA44, GATEA45, GATEA46, GATEA47, GATEA48, GATEA49, GATEA5, GATEA50, GATEA51, GATEA52, GATEA53, GATEA54, GATEA55, GATEA56, GATEA57, GATEA58, GATEA59, GATEA60, GATEA61, GATEA62, GATEA63, GATEA64, GATEA65, GATEA66, GATEA67, GATEA68, GATEA69, GATEA70, GATEA71, GATEA72, GATEA73, GATEA74, GATEA75, GATEA76, GATEA77, GATEA78, GATEA79, GATEA80, GATEA81, GATEA82, GATEA83, GATEA84, GATEA85, GATEA86, GATEA87, GATEA88, GATEA89, GATEA90, GATEA91, GATEA92, GATEA93, GATEA94, GATEA95, GATEA96, GATEA97, GATEA98, GATEA99, GATEB100, GATEB101, GATEB102, GATEB103, GATEB104, GATEB105, GATEB106, GATEB107, GATEB108, GATEB109, GATEB110, GATEB111, GATEB112, GATEB2, GATEB21, GATEB22, GATEB23, GATEB24, GATEB25, GATEB26, GATEB27, GATEB28, GATEB29, GATEB3, GATEB30, GATEB31, GATEB32, GATEB33, GATEB34, GATEB35, GATEB36, GATEB37, GATEB38, GATEB39, GATEB4, GATEB40, GATEB41, GATEB42, GATEB43, GATEB44, GATEB45, GATEB46, GATEB47, GATEB48, GATEB49, GATEB5, GATEB50, GATEB51, GATEB52, GATEB53, GATEB54, GATEB55, GATEB56, GATEB57, GATEB58, GATEB59, GATEB60, GATEB61, GATEB62, GATEB63, GATEB64, GATEB65, GATEB66, GATEB67, GATEB68, GATEB69, GATEB70, GATEB71, GATEB72, GATEB73, GATEB74, GATEB75, GATEB76, GATEB77, GATEB78, GATEB79, GATEB80, GATEB81, GATEB82, GATEB83, GATEB84, GATEB85, GATEB86, GATEB87, GATEB88, GATEB89, GATEB90, GATEB91, GATEB92, GATEB93, GATEB94, GATEB95, GATEB96, GATEB97, GATEB98, GATEB99, LED2, LED3, LED4, LED5, LED6, LED7, LED8, LED9, SOURCEA100, SOURCEA101, SOURCEA102, SOURCEA103, SOURCEA104, SOURCEA105, SOURCEA106, SOURCEA107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: TPTHT, ellajameson-core:PROTOPAD-THT-PAD
- added JD100, JD101, JD102, JD103, JD104, JD105, JD106, JD107, JD108, JD109, JD110, JD111, JD112, JD2, JD21, JD22, JD23, JD24, JD25, JD26, JD27, JD28, JD29, JD3, JD30, JD31, JD32, JD33, JD34, JD35, JD36, JD37, JD38, JD39, JD4, JD40, JD41, JD42, JD43, JD44, JD45, JD46, JD47, JD48, JD49, JD5, JD50, JD51, JD52, JD53, JD54, JD55, JD56, JD57, JD58, JD59, JD60, JD61, JD62, JD63, JD64, JD65, JD66, JD67, JD68, JD69, JD70, JD71, JD72, JD73, JD74, JD75, JD76, JD77, JD78, JD79, JD80, JD81, JD82, JD83, JD84, JD85, JD86, JD87, JD88, JD89, JD90, JD91, JD92, JD93, JD94, JD95, JD96, JD97, JD98, JD99, JN100, JN101, JN102, JN103, JN104, JN105, JN106, JN107, JN108, JN109, JN110, JN111, JN112, JN2, JN21, JN22, JN23, JN24, JN25, JN26, JN27, JN28, JN29, JN3, JN30, JN31, JN32, JN33, JN34, JN35, JN36, JN37, JN38, JN39, JN4, JN40, JN41, JN42, JN43, JN44, JN45, JN46, JN47, JN48, JN49, JN5, JN50, JN51, JN52, JN53, JN54, JN55, JN56, JN57, JN58, JN59, JN60, JN61, JN62, JN63, JN64, JN65, JN66, JN67, JN68, JN69, JN70, JN71, JN72, JN73, JN74, JN75, JN76, JN77, JN78, JN79, JN80, JN81, JN82, JN83, JN84, JN85, JN86, JN87, JN88, JN89, JN90, JN91, JN92, JN93, JN94, JN95, JN96, JN97, JN98, JN99, JP100, JP101, JP102, JP103, JP104, JP105, JP106, JP107, JP108, JP109, JP110, JP111, JP112, JP2, JP21, JP22, JP23, JP24, JP25, JP26, JP27, JP28, JP29, JP3, JP30, JP31, JP32, JP33, JP34, JP35, JP36, JP37, JP38, JP39, JP4, JP40, JP41, JP42, JP43, JP44, JP45, JP46, JP47, JP48, JP49, JP5, JP50, JP51, JP52, JP53, JP54, JP55, JP56, JP57, JP58, JP59, JP60, JP61, JP62, JP63, JP64, JP65, JP66, JP67, JP68, JP69, JP70, JP71, JP72, JP73, JP74, JP75, JP76, JP77, JP78, JP79, JP80, JP81, JP82, JP83, JP84, JP85, JP86, JP87, JP88, JP89, JP90, JP91, JP92, JP93, JP94, JP95, JP96, JP97, JP98, JP99, JS100, JS101, JS102, JS103, JS104, JS105, JS106, JS107, JS108, JS109, JS110, JS111, JS112, JS2, JS21, JS22, JS23, JS24, JS25, JS26, JS27, JS28, JS29, JS3, JS30, JS31, JS32, JS33, JS34, JS35, JS36, JS37, JS38, JS39, JS4, JS40, JS41, JS42, JS43, JS44, JS45, JS46, JS47, JS48, JS49, JS5, JS50, JS51, JS52, JS53, JS54, JS55, JS56, JS57, JS58, JS59, JS60, JS61, JS62, JS63, JS64, JS65, JS66, JS67, JS68, JS69, JS70, JS71, JS72, JS73, JS74, JS75, JS76, JS77, JS78, JS79, JS80, JS81, JS82, JS83, JS84, JS85, JS86, JS87, JS88, JS89, JS90, JS91, JS92, JS93, JS94, JS95, JS96, JS97, JS98, JS99: SJ_NO_THIN, ellajameson-core:SJ_2S-NO-THIN
- added Q100, Q101, Q102, Q103, Q104, Q105, Q106, Q107, Q108, Q109, Q110, Q111, Q112, Q113, Q114, Q115, Q116, Q117, Q118, Q119, Q120, Q2, Q25, Q26, Q27, Q28, Q29, Q3, Q30, Q31, Q32, Q33, Q34, Q35, Q36, Q37, Q38, Q39, Q4, Q40, Q41, Q42, Q43, Q44, Q45, Q46, Q47, Q48, Q49, Q5, Q50, Q51, Q52, Q53, Q54, Q55, Q56, Q57, Q58, Q59, Q6, Q60, Q61, Q62, Q63, Q64, Q65, Q66, Q67, Q68, Q69, Q7, Q70, Q71, Q72, Q73, Q74, Q75, Q76, Q77, Q78, Q79, Q8, Q80, Q81, Q82, Q83, Q84, Q85, Q86, Q87, Q88, Q89, Q9, Q90, Q91, Q92, Q93, Q94, Q95, Q96, Q97, Q98, Q99: 2N7002, ellajameson-core:SOT23
- added R100, R101, R102, R103, R104, R105, R106, R107, R108, R109, R110, R111, R112, R113, R114, R115, R116, R117, R118, R119, R120, R121, R122, R123, R124, R125, R126, R127, R128, R129, R130, R131, R132, R25, R26, R27, R28, R29, R30, R31, R32, R33, R34, R35, R36, R37, R38, R39, R40, R41, R42, R43, R44, R45, R46, R47, R48, R49, R50, R51, R52, R53, R54, R55, R56, R57, R58, R59, R60, R61, R62, R63, R64, R65, R66, R67, R68, R69, R70, R71, R72, R73, R74, R79, R80, R83, R84, R87, R88, R91, R92, R95, R96, R97, R98, R99: 10k, ellajameson-core:R0603
- added R2, R3, R4, R5, R6, R7, R8, R9: 330, ellajameson-core:R0603
- added U$1, U$104, U$108, U$112, U$116, U$120, U$124, U$14, U$168, U$172, U$176, U$18, U$180, U$184, U$188, U$192, U$196, U$204, U$206, U$21, U$210, U$214, U$218, U$222, U$226, U$230, U$234, U$238, U$242, U$246, U$25, U$250, U$254, U$258, U$262, U$266, U$270, U$278, U$286, U$29, U$290, U$294, U$298, U$302, U$306, U$310, U$314, U$318, U$322, U$326, U$330, U$34, U$340, U$344, U$38, U$42, U$46, U$49, U$53, U$57, U$61, U$74, U$78, U$82, U$86, U$90, U$94: PROTOPADTHT, ellajameson-core:PROTOPAD-THT
- added U$10, U$105, U$106, U$109, U$110, U$113, U$114, U$117, U$118, U$12, U$121, U$122, U$125, U$126, U$134, U$136, U$15, U$16, U$169, U$170, U$173, U$174, U$177, U$178, U$181, U$182, U$185, U$186, U$189, U$19, U$190, U$193, U$194, U$197, U$198, U$2, U$20, U$201, U$205, U$207, U$208, U$211, U$212, U$215, U$216, U$219, U$22, U$220, U$223, U$224, U$227, U$228, U$23, U$231, U$232, U$235, U$236, U$239, U$240, U$243, U$244, U$247, U$248, U$251, U$252, U$255, U$256, U$259, U$26, U$260, U$263, U$264, U$267, U$268, U$27, U$271, U$272, U$274, U$275, U$279, U$280, U$283, U$287, U$288, U$291, U$292, U$295, U$296, U$299, U$3, U$30, U$300, U$303, U$304, U$307, U$308, U$31, U$311, U$312, U$315, U$316, U$319, U$320, U$323, U$324, U$327, U$328, U$331, U$332, U$341, U$342, U$345, U$346, U$35, U$36, U$39, U$40, U$43, U$44, U$47, U$48, U$5, U$50, U$51, U$54, U$55, U$58, U$59, U$62, U$63, U$65, U$67, U$69, U$7, U$71, U$75, U$76, U$79, U$80, U$83, U$84, U$87, U$88, U$91, U$92, U$95, U$96, U$98: (no value), ellajameson-core:PROTOPAD-BETWEEN
- added U$107, U$11, U$111, U$115, U$119, U$123, U$127, U$13, U$135, U$137, U$17, U$171, U$175, U$179, U$183, U$187, U$191, U$195, U$199, U$203, U$209, U$213, U$217, U$221, U$225, U$229, U$233, U$237, U$24, U$241, U$245, U$249, U$253, U$257, U$261, U$265, U$269, U$273, U$276, U$277, U$28, U$281, U$285, U$289, U$293, U$297, U$301, U$305, U$309, U$313, U$317, U$32, U$321, U$325, U$329, U$33, U$333, U$343, U$347, U$37, U$4, U$41, U$45, U$52, U$56, U$6, U$60, U$64, U$66, U$68, U$70, U$72, U$73, U$77, U$8, U$81, U$85, U$89, U$9, U$93, U$97, U$99: (no value), ellajameson-core:PROTOPAD-CENTER
- B1, B2, B3, B4, B5, B6, VCC1, VCC2, VCC3, VIN+1, VIN-1, VSS1, VSS2, VSS3: device ellajameson-core:PROTOPAD-THT -> ellajameson-core:PROTOPAD-THT-PAD
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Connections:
- new net N$10: D3.A, R3.1
- new net N$100: JP4.2, R27.1
- new net N$101: JN4.2, JS4.2, Q27.2, SOURCEA4.P1, SOURCEB4.P1
- new net N$102: DRAINA4.P1, DRAINB4.P1, JD3.1, JD4.2, JP4.1, JS51.1, Q27.3
- new net N$103: GATEA4.P1, GATEB4.P1, Q27.1
- new net N$104: JP5.2, R28.1
- new net N$105: JN5.2, JS5.2, Q28.2, SOURCEA5.P1, SOURCEB5.P1
- new net N$106: DRAINA5.P1, DRAINB5.P1, JD4.1, JD5.2, JP5.1, JS52.1, Q28.3
- new net N$107: GATEA5.P1, GATEB5.P1, Q28.1
- new net N$108: JP21.2, R29.1
- new net N$109: JN21.2, JS21.2, Q29.2, SOURCEA21.P1, SOURCEB21.P1
- new net N$11: LED3.P1, Q3.1
- new net N$110: DRAINA21.P1, DRAINB21.P1, JD21.2, JD5.1, JP21.1, JS53.1, Q29.3
- new net N$111: GATEA21.P1, GATEB21.P1, Q29.1
- new net N$112: JP22.2, R30.1
- new net N$113: JN22.2, JS22.2, Q30.2, SOURCEA22.P1, SOURCEB22.P1
- new net N$114: DRAINA22.P1, DRAINB22.P1, JD21.1, JD22.2, JP22.1, JS54.1, Q30.3
- new net N$115: GATEA22.P1, GATEB22.P1, Q30.1
- new net N$116: JP23.2, R31.1
- new net N$117: JN23.2, JS23.2, Q31.2, SOURCEA23.P1, SOURCEB23.P1
- new net N$118: DRAINA23.P1, DRAINB23.P1, JD22.1, JD23.2, JP23.1, JS55.1, Q31.3
- new net N$119: GATEA23.P1, GATEB23.P1, Q31.1
- new net N$12: D3.C, Q3.3
- new net N$120: JP24.2, R32.1
- new net N$121: JN24.2, JS24.2, Q32.2, SOURCEA24.P1, SOURCEB24.P1
- new net N$122: DRAINA24.P1, DRAINB24.P1, JD23.1, JD24.2, JP24.1, JS56.1, Q32.3
- new net N$123: GATEA24.P1, GATEB24.P1, Q32.1
- new net N$124: JP25.2, R33.1
- new net N$125: JN25.2, JS25.2, Q33.2, SOURCEA25.P1, SOURCEB25.P1
- new net N$126: DRAINA25.P1, DRAINB25.P1, JD24.1, JD25.2, JP25.1, JS57.1, Q33.3
- new net N$127: GATEA25.P1, GATEB25.P1, Q33.1
- new net N$128: JP26.2, R34.1
- new net N$129: JN26.2, JS26.2, Q34.2, SOURCEA26.P1, SOURCEB26.P1
- new net N$13: D4.A, R4.1
- new net N$130: DRAINA26.P1, DRAINB26.P1, JD25.1, JD26.2, JP26.1, JS58.1, Q34.3
- new net N$131: GATEA26.P1, GATEB26.P1, Q34.1
- new net N$132: JP27.2, R35.1
- new net N$133: JN27.2, JS27.2, Q35.2, SOURCEA27.P1, SOURCEB27.P1
- new net N$134: DRAINA27.P1, DRAINB27.P1, JD26.1, JD27.2, JP27.1, JS59.1, Q35.3
- new net N$135: GATEA27.P1, GATEB27.P1, Q35.1
- new net N$136: JP28.2, R36.1
- new net N$137: JN28.2, JS28.2, Q36.2, SOURCEA28.P1, SOURCEB28.P1
- new net N$138: DRAINA28.P1, DRAINB28.P1, JD27.1, JD28.2, JP28.1, JS60.1, Q36.3
- new net N$139: GATEA28.P1, GATEB28.P1, Q36.1
- new net N$14: LED4.P1, Q4.1
- new net N$140: JP29.2, R37.1
- new net N$141: JN29.2, JS29.2, Q37.2, SOURCEA29.P1, SOURCEB29.P1
- new net N$142: DRAINA29.P1, DRAINB29.P1, JD28.1, JD29.2, JP29.1, JS61.1, Q37.3
- new net N$143: GATEA29.P1, GATEB29.P1, Q37.1
- new net N$144: JP30.2, R38.1
- new net N$145: JN30.2, JS30.2, Q38.2, SOURCEA30.P1, SOURCEB30.P1
- new net N$146: DRAINA30.P1, DRAINB30.P1, JD29.1, JD30.2, JP30.1, JS62.1, Q38.3
- new net N$147: GATEA30.P1, GATEB30.P1, Q38.1
- new net N$148: JP31.2, R39.1
- new net N$149: JN31.2, JS31.2, Q39.2, SOURCEA31.P1, SOURCEB31.P1
- new net N$15: D4.C, Q4.3
- new net N$150: DRAINA31.P1, DRAINB31.P1, JD30.1, JD31.2, JP31.1, JS63.1, Q39.3
- new net N$151: GATEA31.P1, GATEB31.P1, Q39.1
- new net N$152: JP32.2, R40.1
- new net N$153: JN32.2, JS32.2, Q40.2, SOURCEA32.P1, SOURCEB32.P1
- new net N$154: DRAINA32.P1, DRAINB32.P1, JD31.1, JD32.2, JP32.1, JS64.1, Q40.3
- new net N$155: GATEA32.P1, GATEB32.P1, Q40.1
- new net N$156: JP33.2, R41.1
- new net N$157: JN33.2, JS33.2, Q41.2, SOURCEA33.P1, SOURCEB33.P1
- new net N$158: DRAINA33.P1, DRAINB33.P1, JD33.2, JP33.1, JS2.1, Q41.3
- new net N$159: GATEA33.P1, GATEB33.P1, Q41.1
- new net N$16: D5.A, R5.1
- new net N$160: JP34.2, R42.1
- new net N$161: JN34.2, JS34.2, Q42.2, SOURCEA34.P1, SOURCEB34.P1
- new net N$162: DRAINA34.P1, DRAINB34.P1, JD33.1, JD34.2, JP34.1, JS3.1, Q42.3
- new net N$163: GATEA34.P1, GATEB34.P1, Q42.1
- new net N$164: JP35.2, R43.1
- new net N$165: JN35.2, JS35.2, Q43.2, SOURCEA35.P1, SOURCEB35.P1
- new net N$166: DRAINA35.P1, DRAINB35.P1, JD34.1, JD35.2, JP35.1, JS4.1, Q43.3
- new net N$167: GATEA35.P1, GATEB35.P1, Q43.1
- new net N$168: JP36.2, R44.1
- new net N$169: JN36.2, JS36.2, Q44.2, SOURCEA36.P1, SOURCEB36.P1
- new net N$17: LED5.P1, Q5.1
- new net N$170: DRAINA36.P1, DRAINB36.P1, JD35.1, JD36.2, JP36.1, JS5.1, Q44.3
- new net N$171: GATEA36.P1, GATEB36.P1, Q44.1
- new net N$172: JP37.2, R45.1
- new net N$173: JN37.2, JS37.2, Q45.2, SOURCEA37.P1, SOURCEB37.P1
- new net N$174: DRAINA37.P1, DRAINB37.P1, JD36.1, JD37.2, JP37.1, JS21.1, Q45.3
- new net N$175: GATEA37.P1, GATEB37.P1, Q45.1
- new net N$176: JP38.2, R46.1
- new net N$177: JN38.2, JS38.2, Q46.2, SOURCEA38.P1, SOURCEB38.P1
- new net N$178: DRAINA38.P1, DRAINB38.P1, JD37.1, JD38.2, JP38.1, JS22.1, Q46.3
- new net N$179: GATEA38.P1, GATEB38.P1, Q46.1
- new net N$18: D5.C, Q5.3
- new net N$180: JP39.2, R47.1
- new net N$181: JN39.2, JS39.2, Q47.2, SOURCEA39.P1, SOURCEB39.P1
- new net N$182: DRAINA39.P1, DRAINB39.P1, JD38.1, JD39.2, JP39.1, JS23.1, Q47.3
- new net N$183: GATEA39.P1, GATEB39.P1, Q47.1
- new net N$184: JP40.2, R48.1
- new net N$185: JN40.2, JS40.2, Q48.2, SOURCEA40.P1, SOURCEB40.P1
- new net N$186: DRAINA40.P1, DRAINB40.P1, JD39.1, JD40.2, JP40.1, JS24.1, Q48.3
- new net N$187: GATEA40.P1, GATEB40.P1, Q48.1
- new net N$188: JP41.2, R49.1
- new net N$189: JN41.2, JS41.2, Q49.2, SOURCEA41.P1, SOURCEB41.P1
- new net N$19: D6.A, R6.1
- new net N$190: DRAINA41.P1, DRAINB41.P1, JD40.1, JD41.2, JP41.1, JS25.1, Q49.3
- new net N$191: GATEA41.P1, GATEB41.P1, Q49.1
- new net N$192: JP42.2, R50.1
- new net N$193: JN42.2, JS42.2, Q50.2, SOURCEA42.P1, SOURCEB42.P1
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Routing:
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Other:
- board size 77.5 x 99.1 mm -> 83.8 x 99.1 mm
- board text added: "A#"
- board text added: "A1"
- board text added: "B#"
- board text added: "B1"
- board text added: "C#"
- board text added: "C1"
- board text added: "D"
- board text added: "D#"
- board text added: "D1"
- board text added: "E#"
- board text added: "E1"
- board text added: "F#"
- board text added: "F1"
- board text added: "G"
- board text added: "G#"
- board text added: "G1"
- board text added: "H#"
- board text added: "H1"
- board text added: "I#"
- board text added: "I1"
- board text added: "J#"
- board text added: "J1"
- board text added: "K#"
- board text added: "K1"
- board text added: "L#"
- board text added: "L1"
- board text added: "L2"
- board text added: "L3"
- board text added: "L4"
- board text added: "L5"
- board text added: "L6"
- board text added: "L7"
- board text added: "L8"
- board text added: "M#"
- board text added: "M1"
- board text added: "N#"
- board text added: "N1"
- board text added: "O#"
- board text added: "O1"
- board text added: "P#"
- board text added: "P1"
- board text added: "S"
